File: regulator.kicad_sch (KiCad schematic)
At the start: 19 parts, among them U3 LMR51635, U4 INA169

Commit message: finish layout
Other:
- moved on the sheet: R11, R7, R8, U4

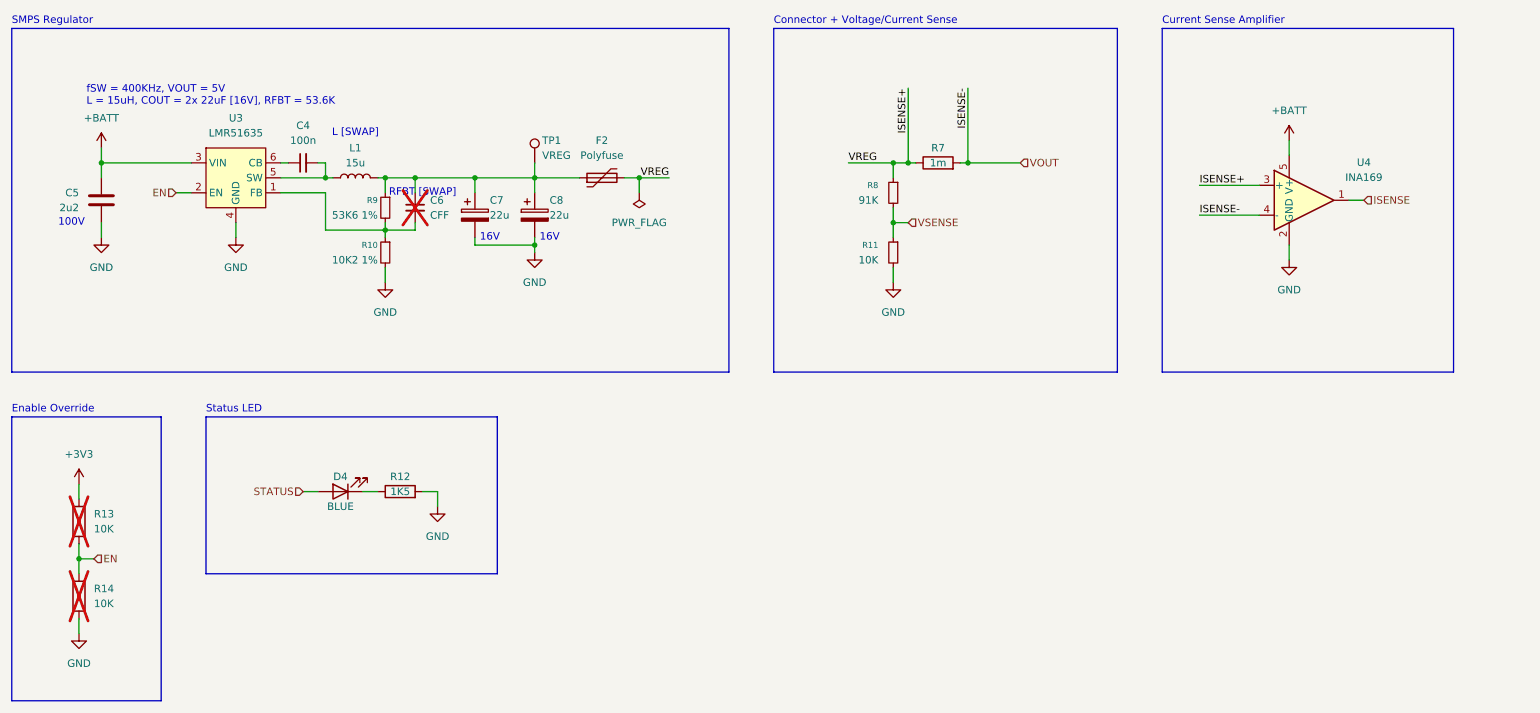
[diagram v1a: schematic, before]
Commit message: optimize components, update schematic pdf
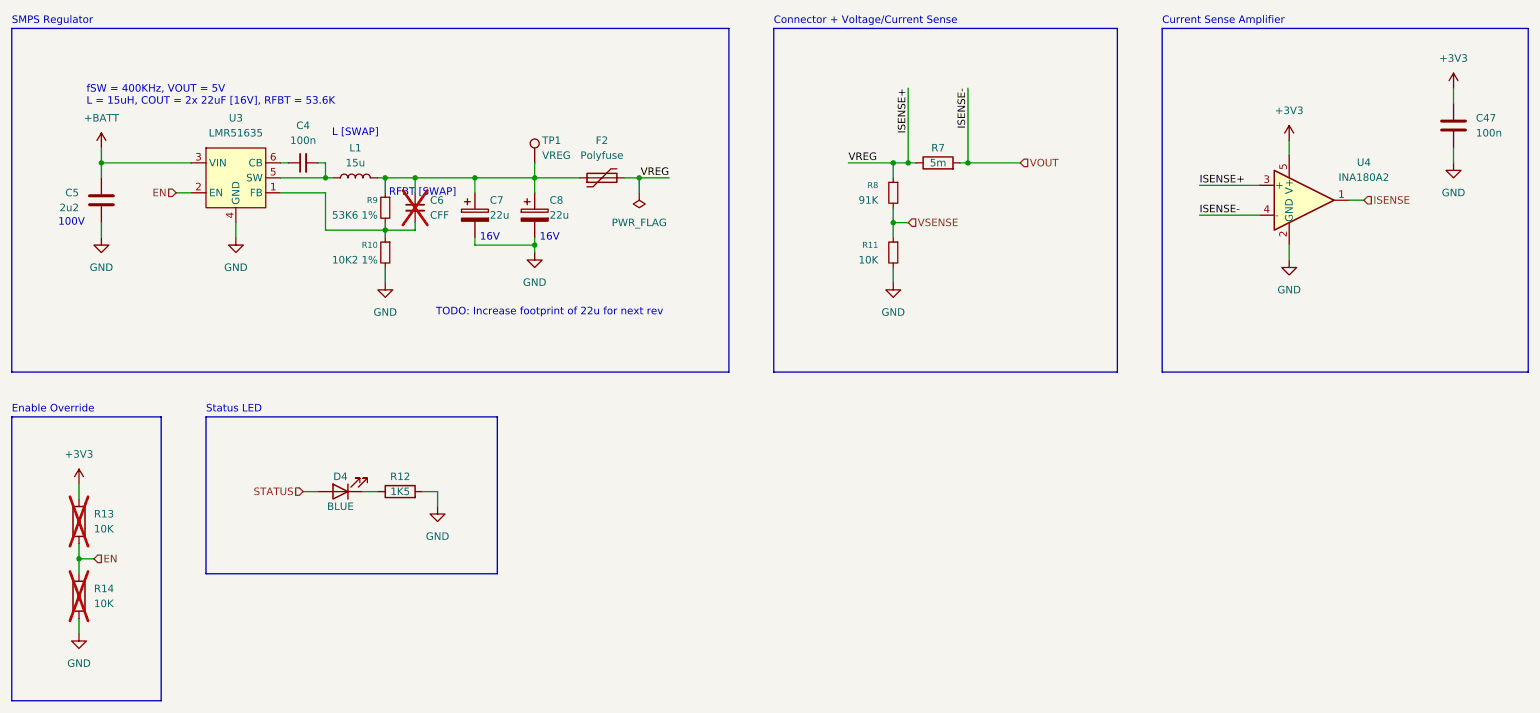
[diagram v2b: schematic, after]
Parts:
- added C47: 100n, Capacitor_SMD:C_0402_1005Metric, symbol Device:C
- R7: value 1m -> 5m
- U4: value INA169 -> INA180A2; symbol Amplifier_Current:INA169 -> Amplifier_Current:INA180A2
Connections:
- net +3V3: now also U4.5 (V+), C47.1
- net +BATT: no longer U4.5 (V+)
- net GND: now also C47.2
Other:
- note added: "TODO: Increase footprint of 22u for next rev"
